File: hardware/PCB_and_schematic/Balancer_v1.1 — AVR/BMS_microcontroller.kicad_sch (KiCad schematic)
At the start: 50 parts, among them J10 RS485, J2 Conn_01x04, J8 ICP, J9 RS485, Q17 BC817, Q18 BC817, Q19 BC817, Q20 BC817, Q21 BC817, Q22 BC817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

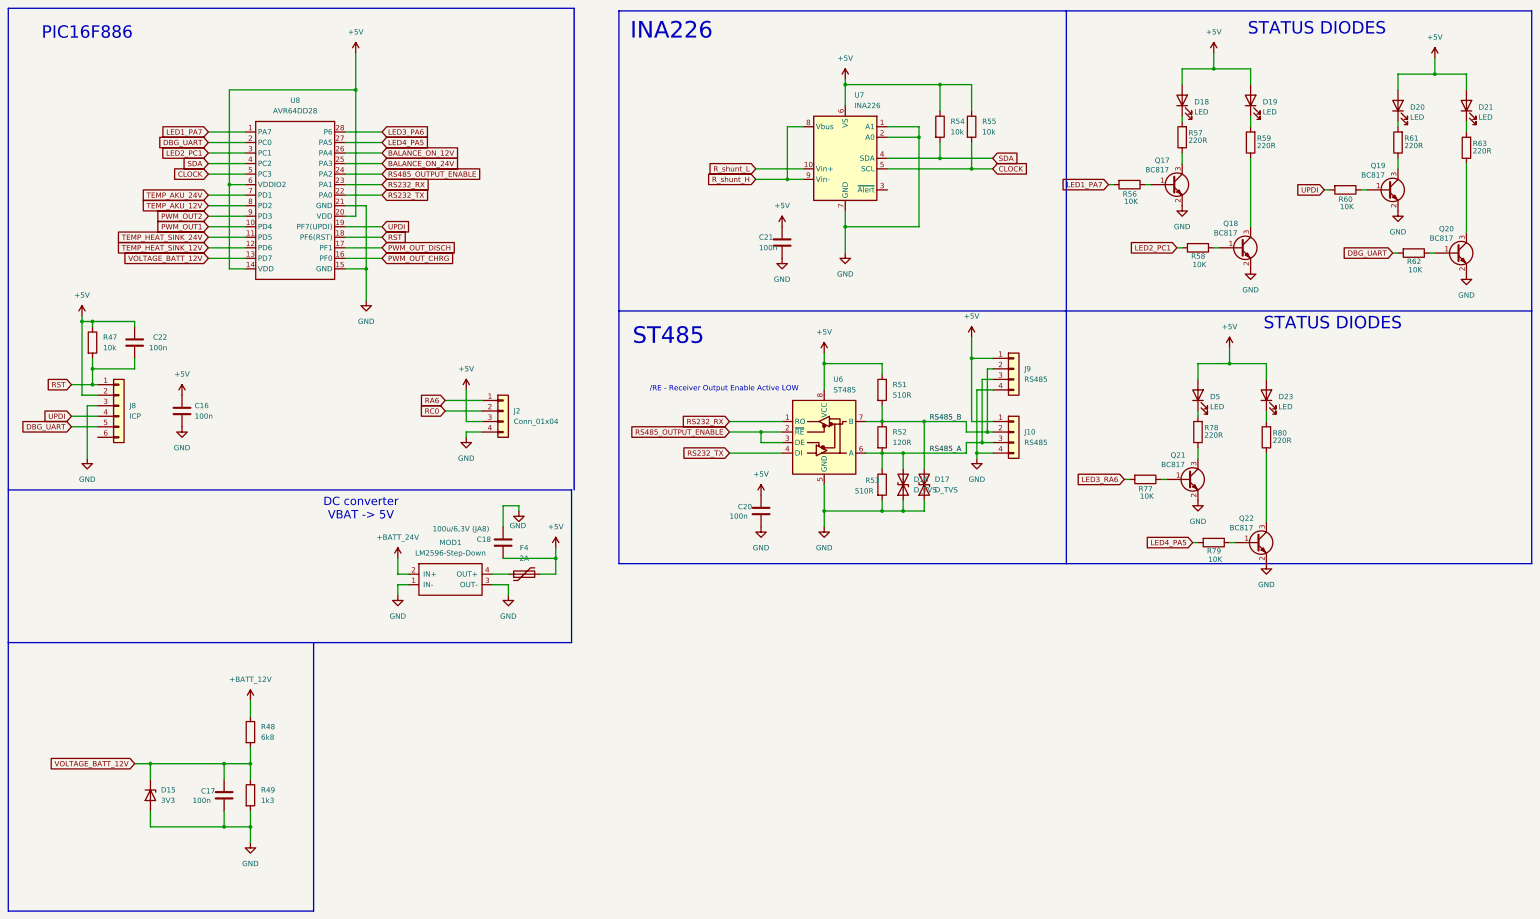
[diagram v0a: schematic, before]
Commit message: change uc on balancer
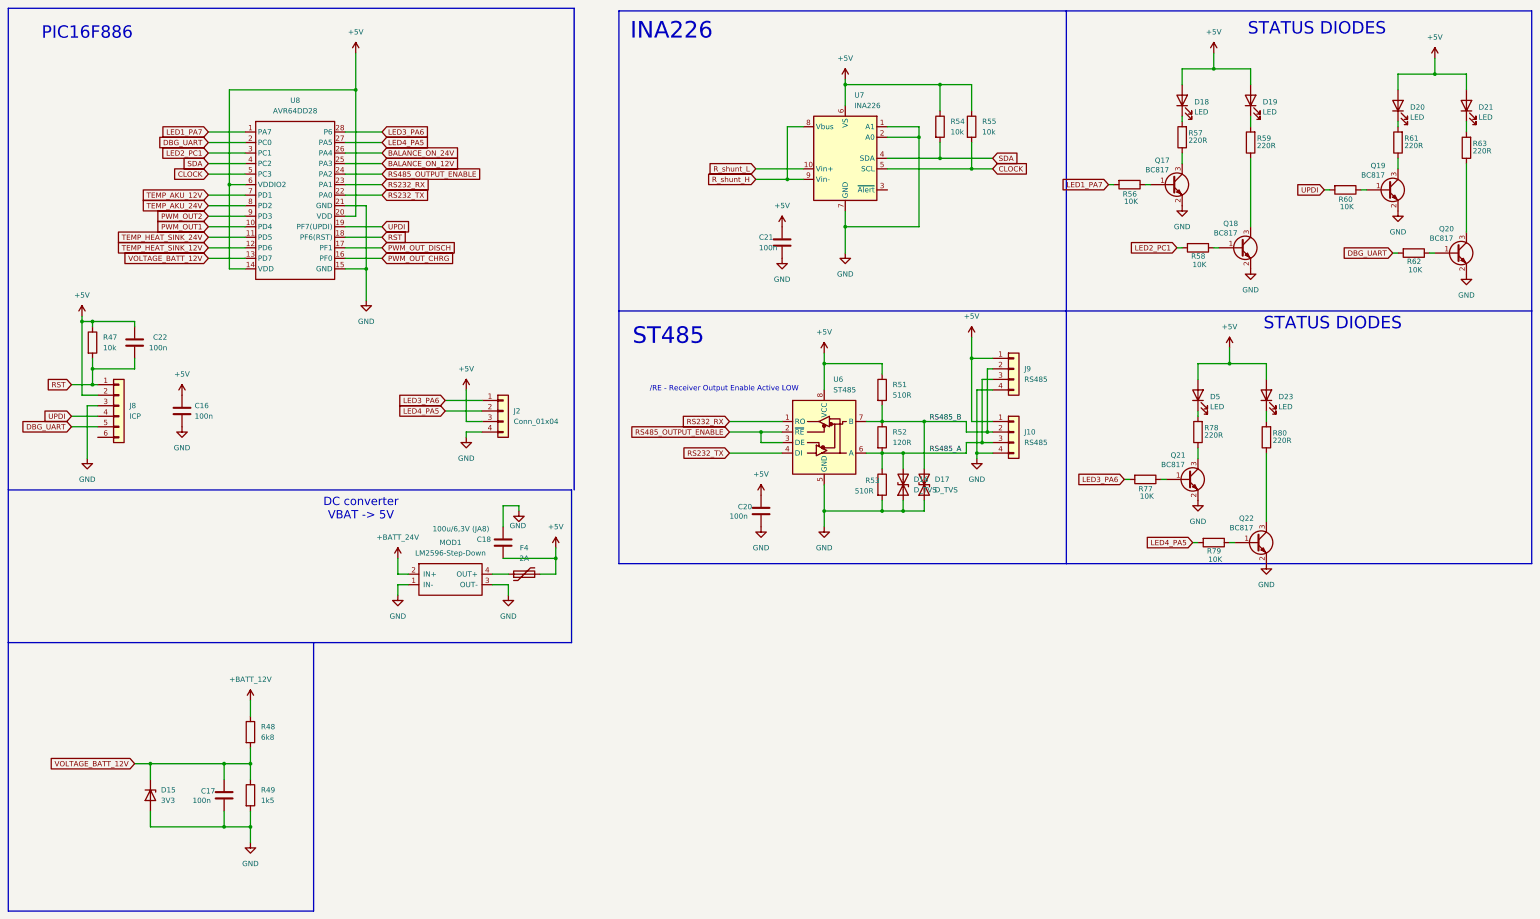
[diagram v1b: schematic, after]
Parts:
- R49: value 1k3 -> 1k5
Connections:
- net LED3_RA6 is gone; now on net LED3_PA6: R77.2
- net RA6 is gone; now on net LED3_PA6: J2.1 (Pin_1)
- net RC0 is gone; now on net LED4_PA5: J2.2 (Pin_2)
- net BALANCE_ON_12V: now also U8.25 (PA3); no longer U8.26 (PA4)
- net BALANCE_ON_24V: now also U8.26 (PA4); no longer U8.25 (PA3)
- net TEMP_AKU_12V: now also U8.7 (PD1); no longer U8.8 (PD2)
- net TEMP_AKU_24V: now also U8.8 (PD2); no longer U8.7 (PD1)

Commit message: change with balancer schematic, generate code for avr
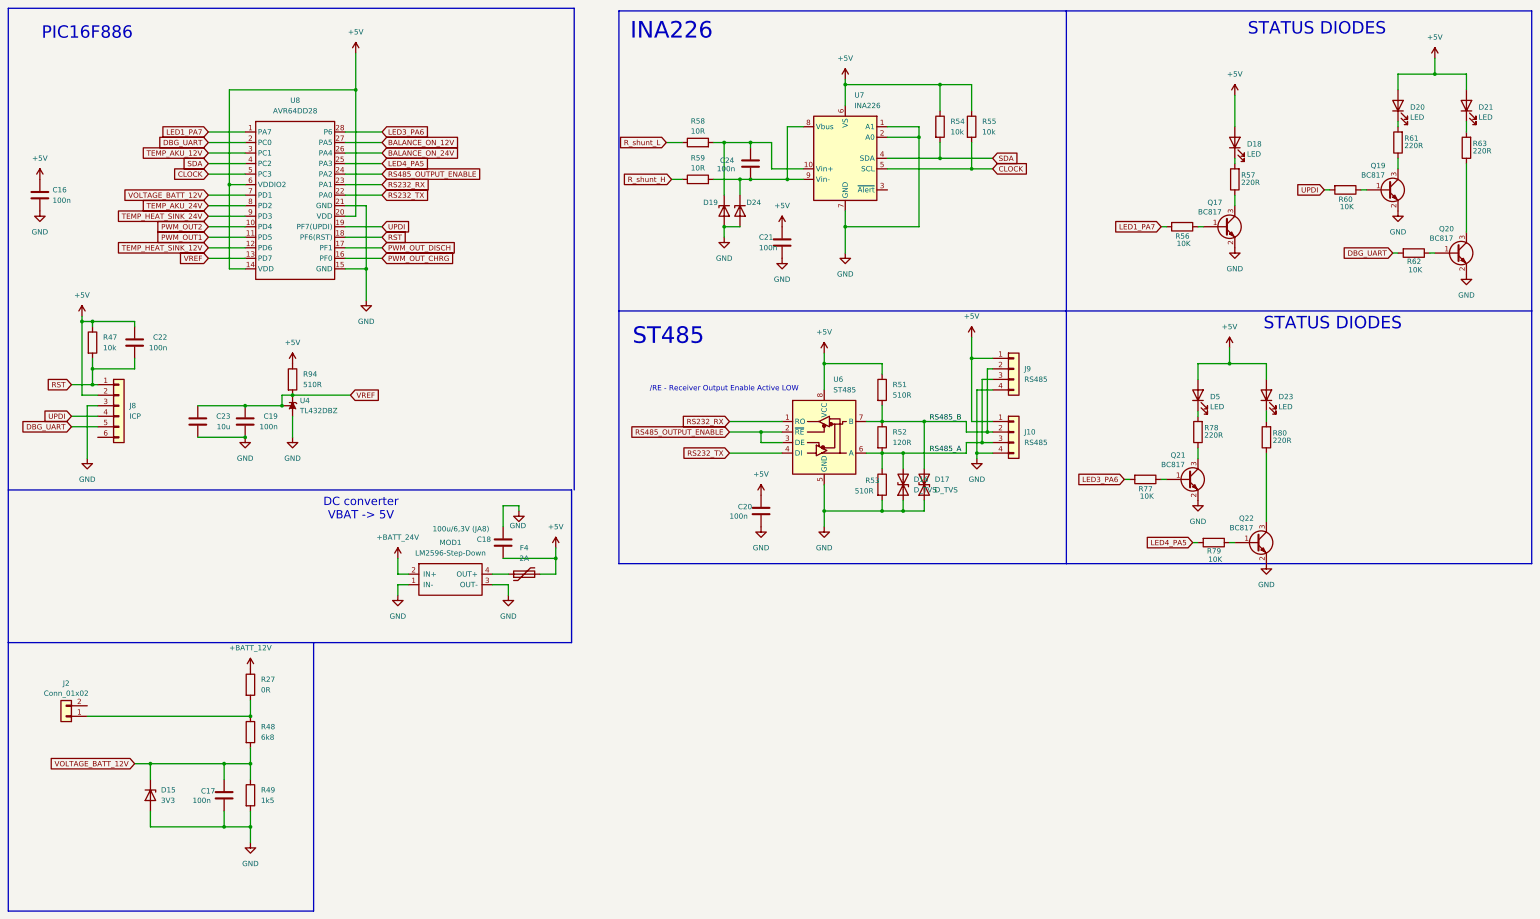
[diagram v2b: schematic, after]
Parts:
- removed D19: LED, LED_THT:LED_D5.0mm, symbol Device:LED
- removed J2: Conn_01x04, Connector_PinHeader_2.54mm:PinHeader_1x04_P2.54mm_Vertical, symbol Connector_Generic:Conn_01x04
- removed Q18: BC817, Package_TO_SOT_SMD:SOT-23, symbol Transistor_BJT:BC817
- added C19: 100n, Capacitor_SMD:C_0805_2012Metric_Pad1.18x1.45mm_HandSolder, symbol Device:C
- added C23: 10u, Capacitor_SMD:C_0805_2012Metric_Pad1.18x1.45mm_HandSolder, symbol Device:C
- added C24: 100n, Resistor_SMD:R_0805_2012Metric_Pad1.20x1.40mm_HandSolder, symbol Device:C
- added D19, D24: PTVS5V0Z1USK, Diode_SMD:D_SOD-123, symbol Diode:PTVS5V0Z1USK
- added J2: Conn_01x02, Connector_JST:JST_XA_B02B-XASK-1-A_1x02_P2.50mm_Vertical, symbol Connector_Generic:Conn_01x02
- added R27: 0R, Resistor_SMD:R_0805_2012Metric_Pad1.20x1.40mm_HandSolder, symbol Device:R
- added R94: 510R, Resistor_SMD:R_0805_2012Metric_Pad1.20x1.40mm_HandSolder, symbol Device:R
- added U4: TL432DBZ, Package_TO_SOT_SMD:SOT-23, symbol Reference_Voltage:TL432DBZ
- R58: value 10K -> 10R
- R59: value 220R -> 10R
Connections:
- net +5V: now also R94.1
- net +BATT_12V: now also R27.1; no longer R48.1
- net BALANCE_ON_12V: now also U8.27 (PA5); no longer U8.25 (PA3)
- net GND: now also C19.2, C23.2, D19.2 (A), D24.2 (A), U4.3 (A)
- net LED4_PA5: now also U8.25 (PA3); no longer U8.27 (PA5)
- net PWM_OUT1: now also U8.11 (PD5); no longer U8.10 (PD4)
- net PWM_OUT2: now also U8.10 (PD4); no longer U8.9 (PD3)
- net R_shunt_H: now also R59.1; no longer U7.8 (Vbus), U7.9 (Vin-)
- net R_shunt_L: now also R58.1; no longer U7.10 (Vin+)
- net TEMP_AKU_12V: now also U8.3 (PC1); no longer U8.7 (PD1)
- net TEMP_HEAT_SINK_24V: now also U8.9 (PD3); no longer U8.11 (PD5)
- net VOLTAGE_BATT_12V: now also U8.7 (PD1); no longer U8.13 (PD7)
- net at R59.2: now also U7.8 (Vbus), U7.9 (Vin-), C24.2, D24.1 (K)
- net LED2_PC1: no longer names the net of R58.2
- net LED2_PC1: now also U7.10 (Vin+), C24.1, D19.1 (K); no longer U8.3 (PC1)
- new net: J2.1 (Pin_1), R27.2, R48.1
- new net VREF: C19.1, C23.1, R94.2, U4.1 (REF), U4.2 (K), U8.13 (PD7)
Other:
- moved on the sheet: C16, D18, Q17, R56, R57

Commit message: ADD INA PROTECTION
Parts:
- added C25: 100n, Resistor_SMD:R_0805_2012Metric_Pad1.20x1.40mm_HandSolder, symbol Device:C
- added D25: PTVS5V0Z1USK, Diode_SMD:D_SOD-123, symbol Diode:PTVS5V0Z1USK
- added R26: 0R, Resistor_SMD:R_0805_2012Metric_Pad1.20x1.40mm_HandSolder, symbol Device:R
- added R41: 10R, Resistor_SMD:R_0805_2012Metric_Pad1.20x1.40mm_HandSolder, symbol Device:R
- J2: value Conn_01x02 -> VOLTAGE_3WIRE
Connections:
- net GND: now also C25.2, D25.2 (A)
- net at C24.2, D24.1 (K), R59.2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: now also R26.1; no longer U7.8 (Vbus)
- net VOLTAGE_BATT_24V_3W: now reaches J2.2 (Pin_2)
- net VOLTAGE_BATT_24V_3W: now also R41.1
- new net: C25.1, D25.1 (K), R26.2, R41.2, U7.8 (Vbus)
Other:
- moved on the sheet: C21, R54, R55, U7

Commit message: Add 3D PCB view
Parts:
- D16, D17: footprint Diode_SMD:D_SMA -> Diode_SMD:Nexperia_CFP3_SOD-123W
- F4: footprint Fuse:Fuse_2512_6332Metric_Pad1.52x3.35mm_HandSolder -> Fuse:Fuse_2920_7451Metric_Pad2.10x5.45mm_HandSolder
- J2: footprint Connector_JST:JST_XA_B02B-XASK-1-A_1x02_P2.50mm_Vertical -> Connector_JST:JST_XH_B2B-XH-A_1x02_P2.50mm_Vertical
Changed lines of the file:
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@@
 			)
 		)
-		(property "Footprint" "Diode_SMD:D_SMA"
+		(property "Footprint" "Diode_SMD:Nexperia_CFP3_SOD-123W"
 			(at 245.11 143.51 0)
 			(effects
@@
 			)
 		)
-		(property "Footprint" "Fuse:Fuse_2512_6332Metric_Pad1.52x3.35mm_HandSolder"
+		(property "Footprint" "Fuse:Fuse_2920_7451Metric_Pad2.10x5.45mm_HandSolder"
 			(at 153.67 163.83 0)
 			(effects
@@
 			)
 		)
-		(property "Footprint" "Connector_JST:JST_XA_B02B-XASK-1-A_1x02_P2.50mm_Vertical"
+		(property "Footprint" "Connector_JST:JST_XH_B2B-XH-A_1x02_P2.50mm_Vertical"
 			(at 38.1 199.39 0)
 			(effects
@@
 			)
 		)
-		(property "Footprint" "Diode_SMD:D_SMA"
+		(property "Footprint" "Diode_SMD:Nexperia_CFP3_SOD-123W"
 			(at 240.03 143.51 0)
 			(effects

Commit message: values update
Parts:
- C17: value 100n -> 470n
- R49: value 1k5 -> 1k
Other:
- note added: "6k8 1k 1,92V @ 15V"
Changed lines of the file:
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@@
 		)
 	)
+	(text "6k8  1k\n1,92V @ 15V"
+		(exclude_from_sim no)
+		(at 92.71 212.852 0)
+		(effects
+			(font
+				(size 1.27 1.27)
+			)
+		)
+	)
 	(text "INA226\n"
 		(exclude_from_sim no)
@@
 			)
 		)
-		(property "Value" "1k5"
+		(property "Value" "1k"
 			(at 85.09 219.7099 0)
 			(effects
@@
 			)
 		)
-		(property "Value" "100n"
+		(property "Value" "470n"
 			(at 68.58 219.71 0)
 			(effects
